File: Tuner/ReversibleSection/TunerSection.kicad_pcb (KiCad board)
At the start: 2 copper layers, 100 x 100 mm, 109 parts, among them J1 Conn_01x03, J10 Conn_01x02, J11 Conn_02x05_Odd_Even, J12 Conn_01x01, J13 Conn_01x01, J14 Conn_01x01, J15 Conn_01x01, J2 Conn_01x03, J3 Conn_01x03, J4 Conn_01x03, J5 Conn_01x03, J6 Conn_01x03, J7 Conn_01x03, J8 Conn_01x02, J9 Conn_01x02, P10 Conn_01x01, P11 Conn_01x01, P12 Conn_01x01, P2 Conn_01x01, P3 Conn_01x01, P4 Conn_01x01, P5 Conn_01x01, P6 Conn_01x01, P7 Conn_01x01, P8 Conn_01x01, P9 Conn_01x01, U1 MCP23008, U2 ULN2803A

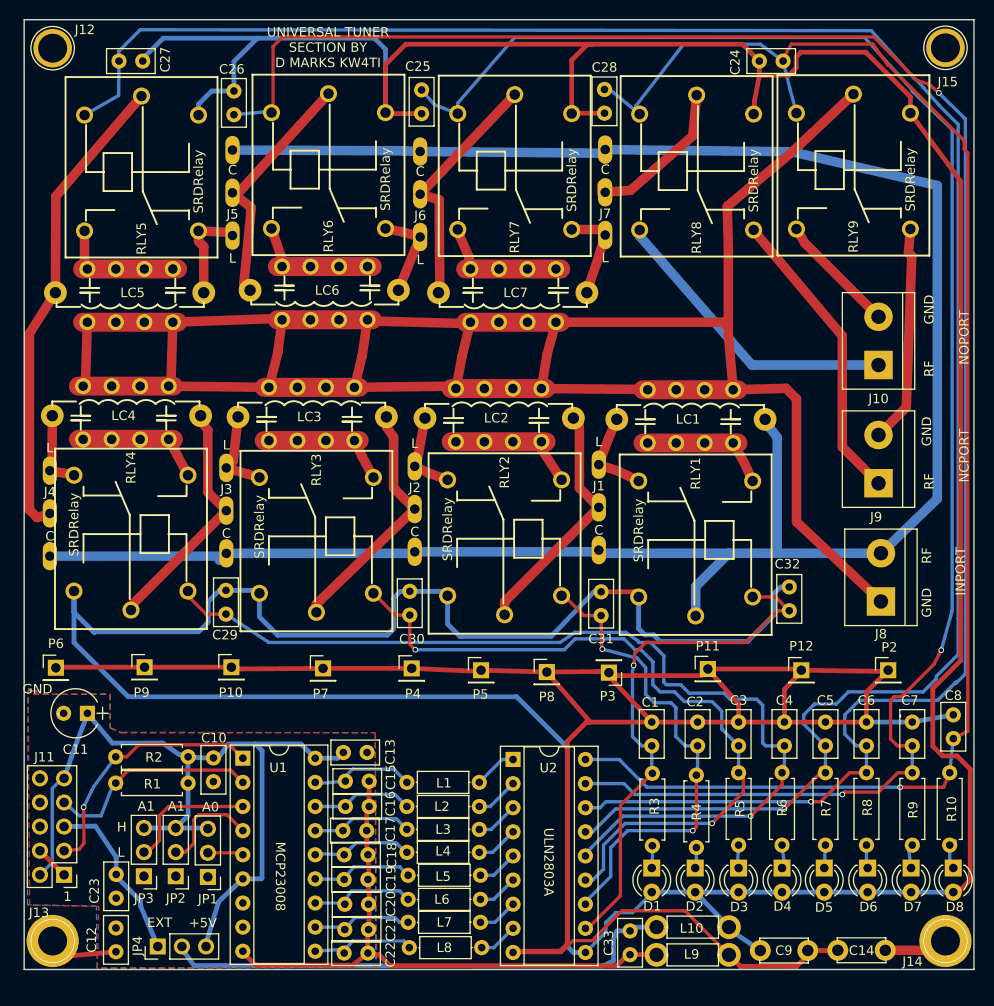
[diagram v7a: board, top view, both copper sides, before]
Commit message: Added boards for SMIH/Schrack Relays
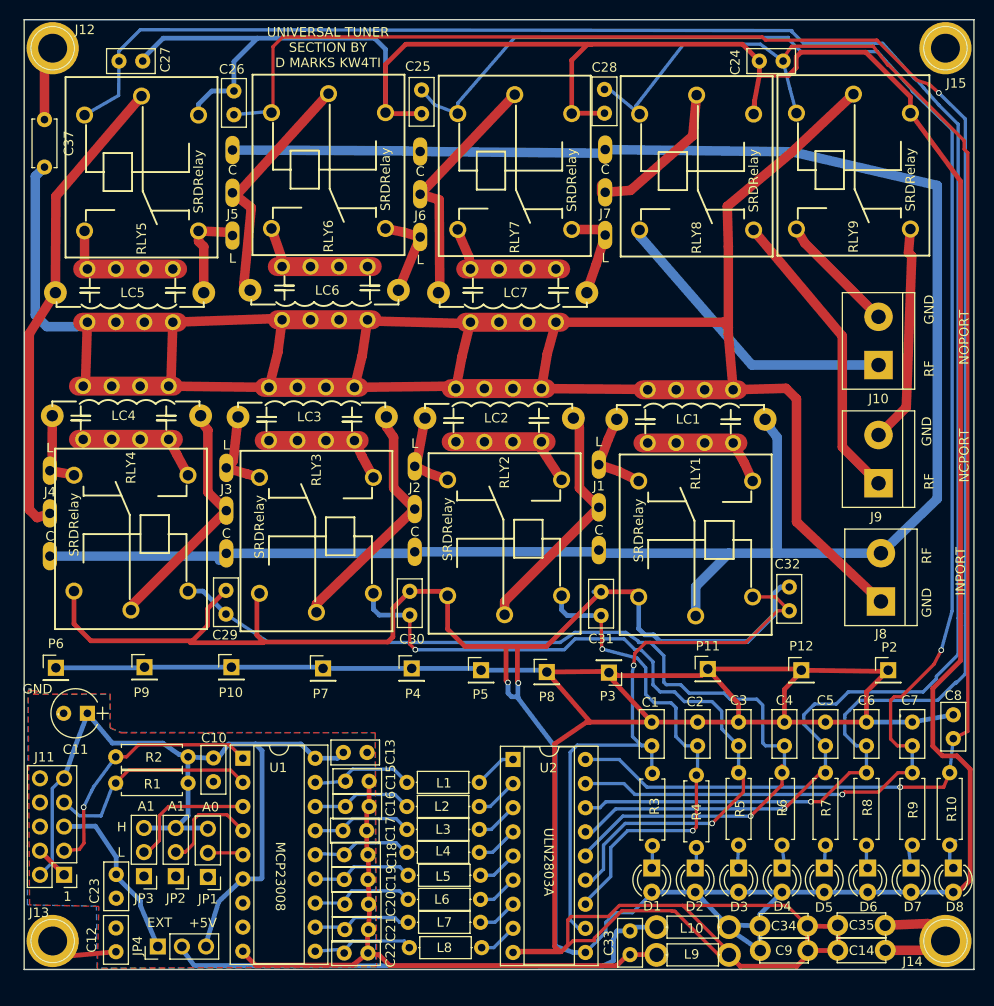
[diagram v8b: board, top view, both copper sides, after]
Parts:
- added C34: 10 nF, Capacitors_THT:C_Disc_D5.0mm_W2.5mm_P5.00mm, F.Cu at (127.5, 145.4)
- added C35: 10 nF, Capacitors_THT:C_Disc_D5.0mm_W2.5mm_P5.00mm, F.Cu at (140.7, 145.3)
- added C37: 10 nF, Capacitors_THT:C_Disc_D5.0mm_W2.5mm_P5.00mm, F.Cu at (52.1, 60.5)
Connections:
- J12 pad 1: (no net) -> Net-(C37-Pad1)
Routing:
- net RLYGND: track 234.6 -> 287.3 mm
- net RLYPWR: track 474.9 -> 449.6 mm, vias 0 -> 2
- net RFGND: track 194.3 -> 216.5 mm
- net Net-(C14-Pad1): track 7.50 -> 17.2 mm
- net RLY1: track 56.1 -> 65.5 mm
- net Net-(C37-Pad1): track 0.00 -> 7.88 mm
- net RLY2: track 51.7 -> 52.9 mm
- net RLY3: track 78.6 -> 79.6 mm
